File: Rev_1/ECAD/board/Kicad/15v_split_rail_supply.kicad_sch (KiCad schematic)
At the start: 0 parts

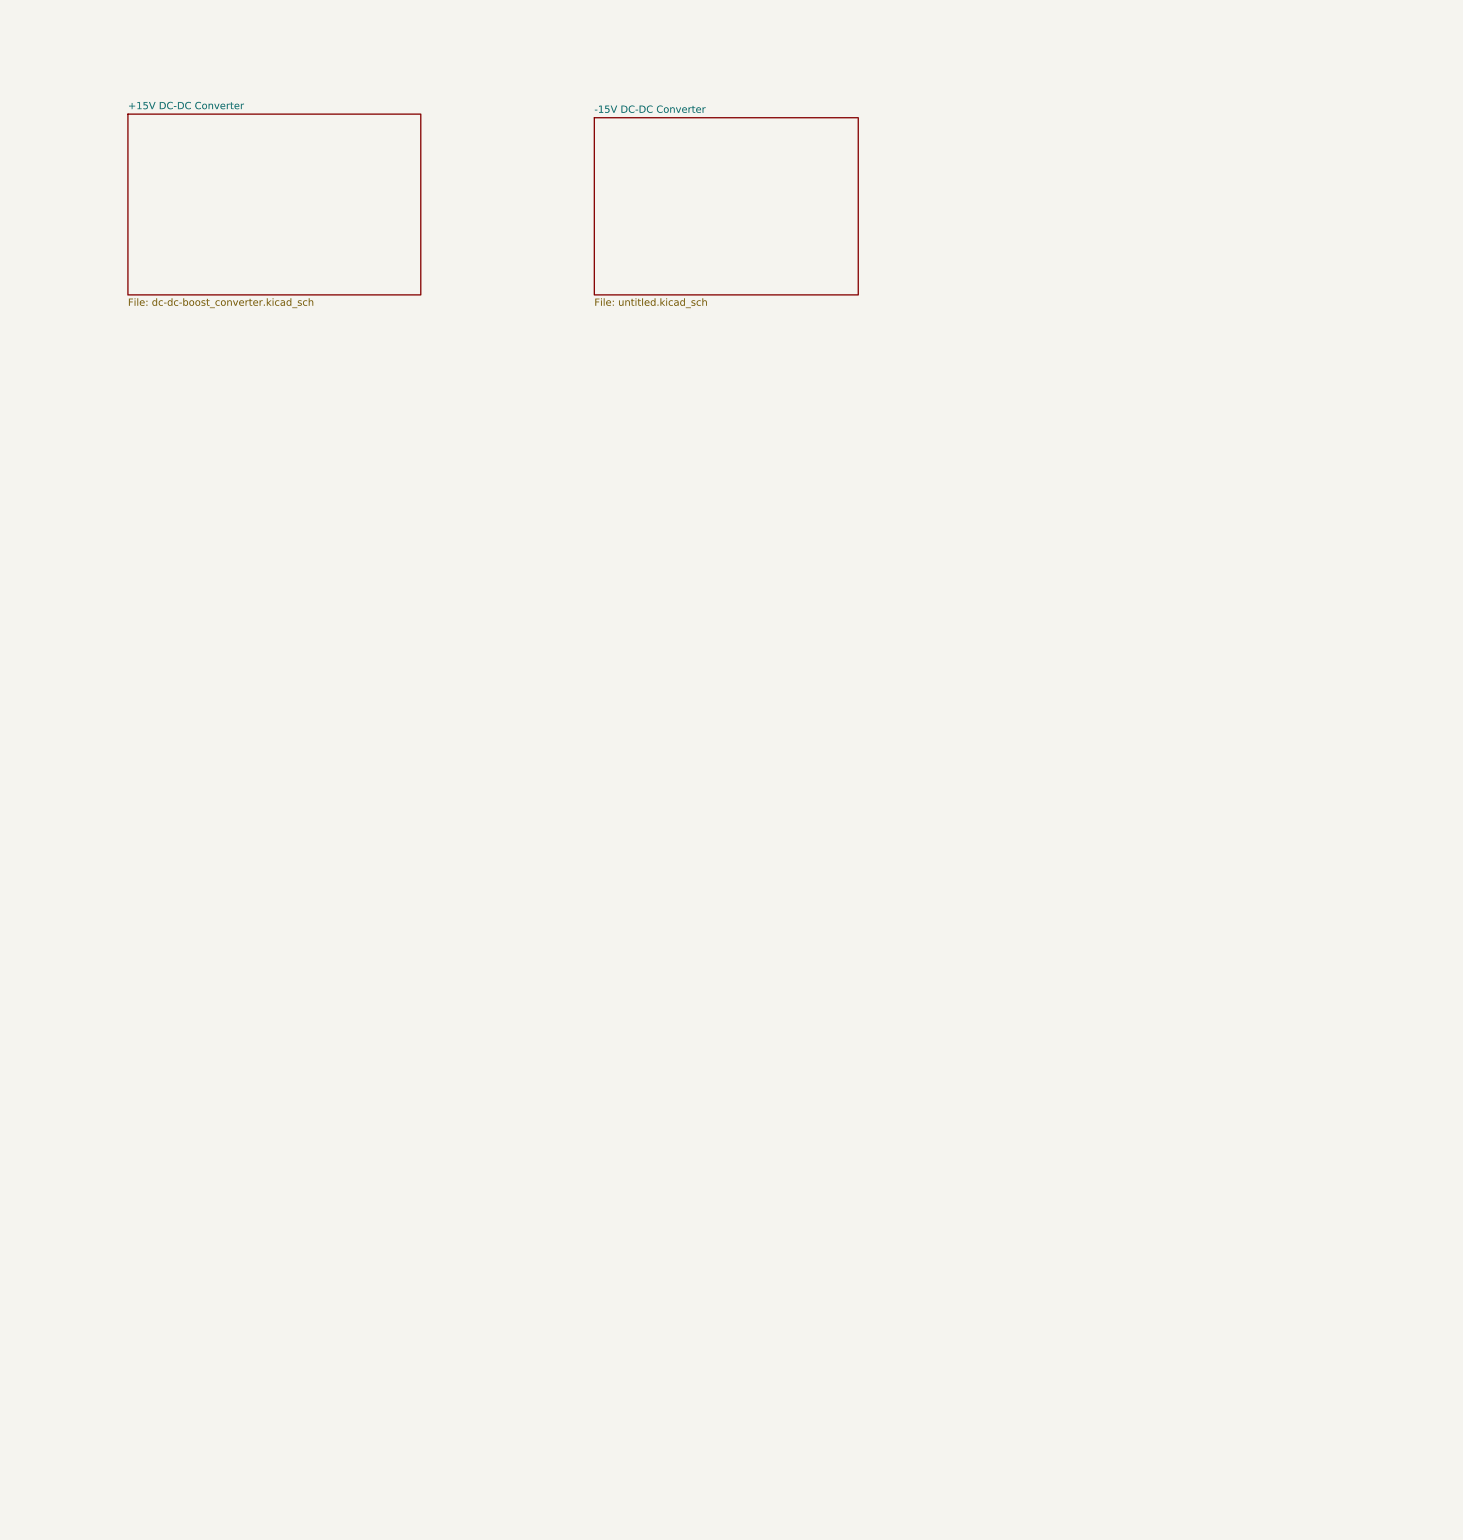
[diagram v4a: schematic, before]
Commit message: -15V schematic is mostly complete
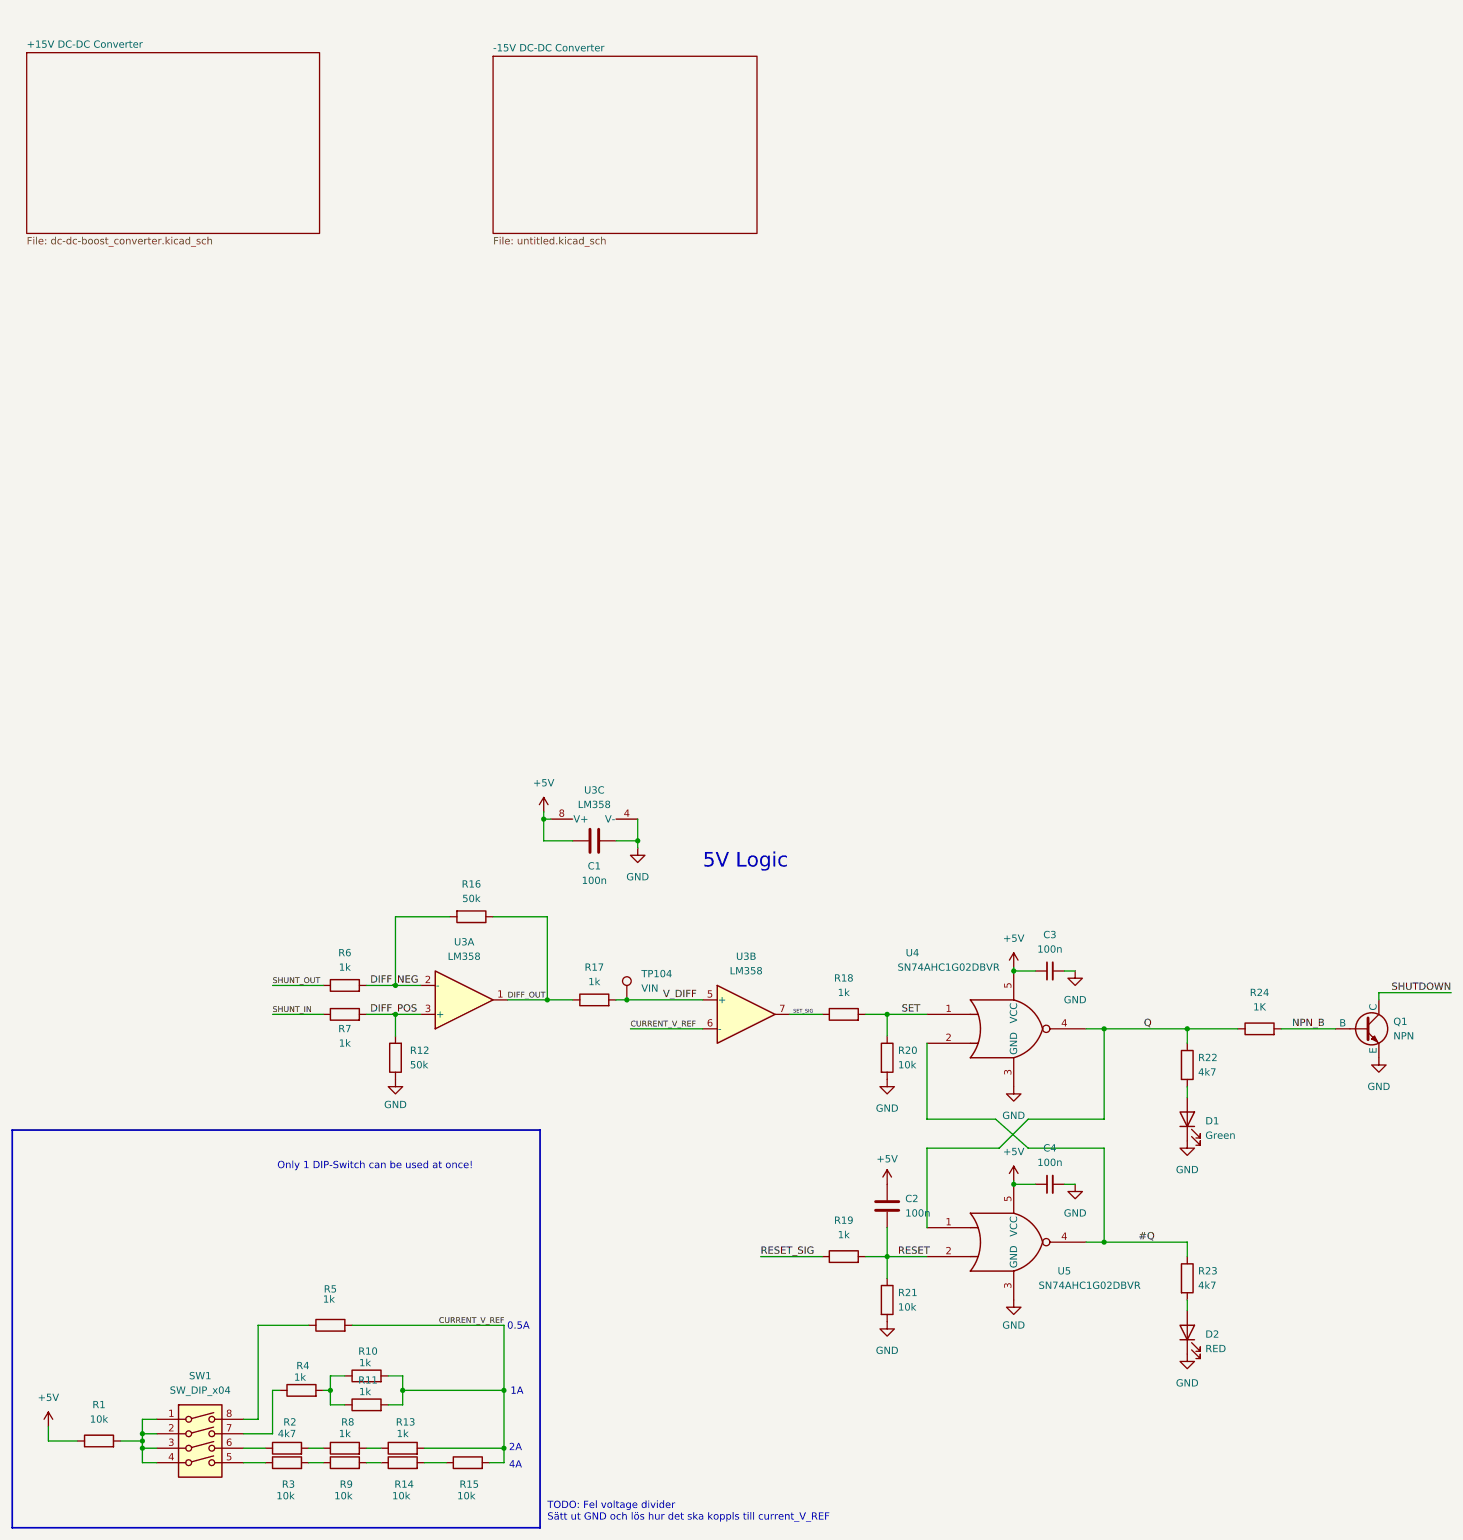
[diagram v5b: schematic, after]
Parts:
- added C1, C2: 100n, Capacitor_SMD:C_0603_1608Metric_Pad1.08x0.95mm_HandSolder, symbol Device:C
- added C3, C4: 100n, Capacitor_SMD:C_0603_1608Metric_Pad1.08x0.95mm_HandSolder, symbol Device:C_Small
- added D1: Green, LED_SMD:LED_0805_2012Metric_Pad1.15x1.40mm_HandSolder, symbol Device:LED
- added D2: RED, LED_SMD:LED_0805_2012Metric_Pad1.15x1.40mm_HandSolder, symbol Device:LED
- added Q1: NPN, Package_TO_SOT_SMD:SOT-23_Handsoldering, symbol Simulation_SPICE:NPN
- added R1, R14, R15, R20, R21, R3, R9: 10k, Resistor_SMD:R_0805_2012Metric_Pad1.20x1.40mm_HandSolder, symbol Device:R
- added R10, R11, R13, R17, R18, R19, R4, R5, R6, R7, R8: 1k, Resistor_SMD:R_0805_2012Metric_Pad1.20x1.40mm_HandSolder, symbol Device:R
- added R12, R16: 50k, Resistor_SMD:R_0603_1608Metric_Pad0.98x0.95mm_HandSolder, symbol Device:R
- added R2, R22, R23: 4k7, Resistor_SMD:R_0805_2012Metric_Pad1.20x1.40mm_HandSolder, symbol Device:R
- added R24: 1K, Resistor_SMD:R_0805_2012Metric_Pad1.20x1.40mm_HandSolder, symbol Device:R
- added SW1: SW_DIP_x04, symbol Switch:SW_DIP_x04
- added TP104: VIN, Connector_Pin:Pin_D0.7mm_L6.5mm_W1.8mm_FlatFork, symbol Connector:TestPoint
- added U3: LM358, Package_SO:SOIC-8_3.9x4.9mm_P1.27mm, symbol Amplifier_Operational:LM358
- added U4, U5: SN74AHC1G02DBVR, Package_TO_SOT_SMD:SOT-23-5_HandSoldering, symbol 74xGxx:74AHC1G02
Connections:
- new net: R1.2, SW1.1, SW1.2, SW1.3, SW1.4
- new net: R10.1, R11.1, R4.2
- new net: D2.2 (A), R23.2
- new net: R13.1, R8.2
- new net: R5.1, SW1.8
- new net: R14.2, R15.1
- new net: R4.1, SW1.7
- new net: R14.1, R9.2
- new net: D1.2 (A), R22.2
- new net: R3.2, R9.1
- new net: R3.1, SW1.5
- new net: R2.1, SW1.6
- new net: R2.2, R8.1
- new net #Q: R23.1, U4.2, U5.4
- new net +5V: C1.2, C2.1, C3.1, C4.1, R1.1, U3.8 (V+), U4.5 (VCC), U5.5 (VCC)
- new net CURRENT_V_REF: R10.2, R11.2, R13.2, R15.2, R5.2, U3.6 (-)
- new net DIFF_NEG: R16.2, R6.2, U3.2 (-)
- new net DIFF_OUT: R16.1, R17.1, U3.1
- new net DIFF_POS: R12.2, R7.2, U3.3 (+)
- new net GND: C1.1, C3.2, C4.2, D1.1 (K), D2.1 (K), Q1.3 (E), R12.1, R20.2, R21.2, U3.4 (V-), U4.3 (GND), U5.3 (GND)
- new net NPN_B: Q1.2 (B), R24.2
- new net Q: R22.1, R24.1, U4.4, U5.1
- new net RESET: C2.2, R19.2, R21.1, U5.2
- new net RESET_SIG: R19.1
- new net SET: R18.2, R20.1, U4.1
- new net SET_SIG: R18.1, U3.7
- new net SHUNT_IN: R7.1
- new net SHUNT_OUT: R6.1
- new net SHUTDOWN: Q1.1 (C)
- new net V_DIFF: R17.2, TP104.1, U3.5 (+)
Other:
- note added: "0.5A"
- note added: "1A"
- note added: "2A"
- note added: "4A"
- note added: "5V Logic"
- note added: "Only 1 DIP-Switch can be used at once!"
- note added: "TODO: Fel voltage divider Sätt ut GND och lös hur det ska koppls till current_V_REF"
